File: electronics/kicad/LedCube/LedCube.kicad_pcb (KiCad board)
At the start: 2 copper layers, 86 x 46 mm, 25 parts, among them J1 Conn_01x03, J2 Conn_01x03, J3 Conn_01x03, J4 Conn_01x04, J5 COM, J6 Conn_01x02, J7 JTAG, U3 ESP32-DevKitM

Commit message: Update kicad gerbers
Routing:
- net D0: track 37.2 -> 40.0 mm
- net D1: track 38.6 -> 40.5 mm
- net D3: track 47.2 -> 46.3 mm
- net D2: track 40.1 -> 40.9 mm
- net GND: vias 6 -> 8

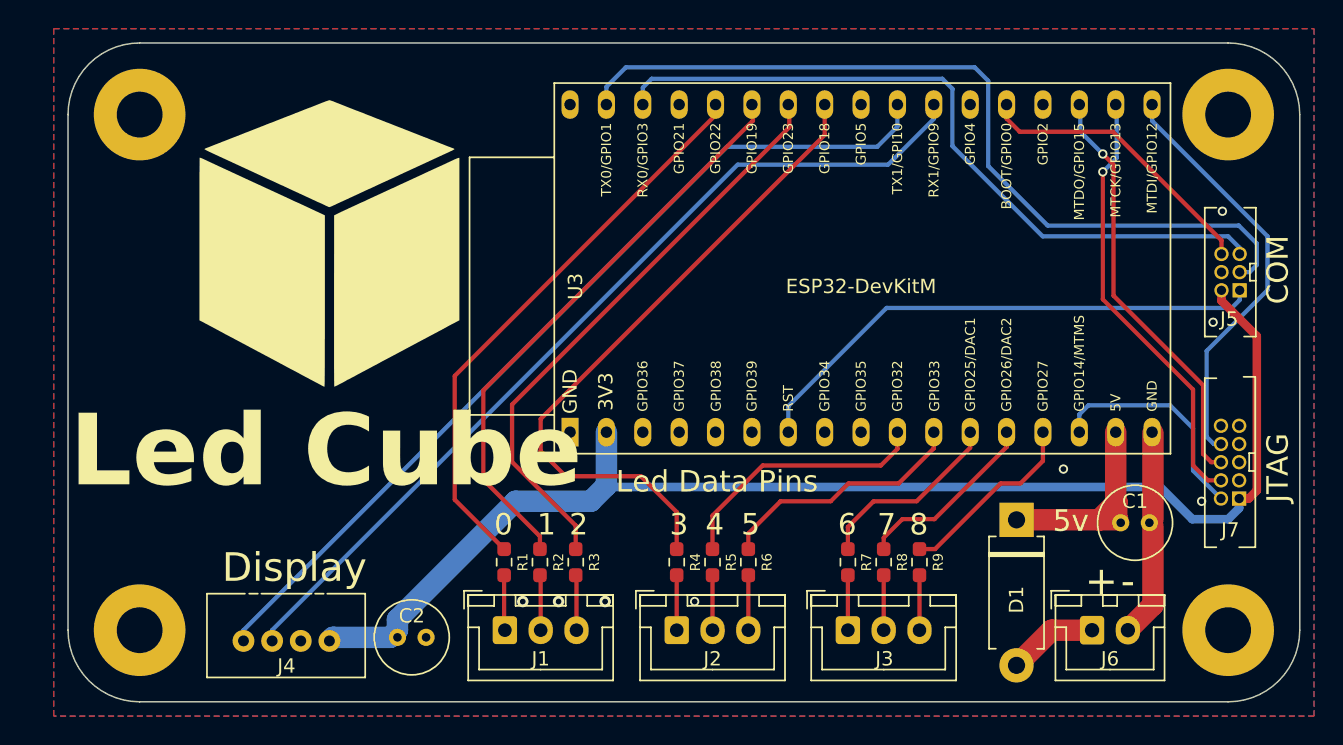
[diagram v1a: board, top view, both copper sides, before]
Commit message: Fix flipped vcc and gnd in KiCad
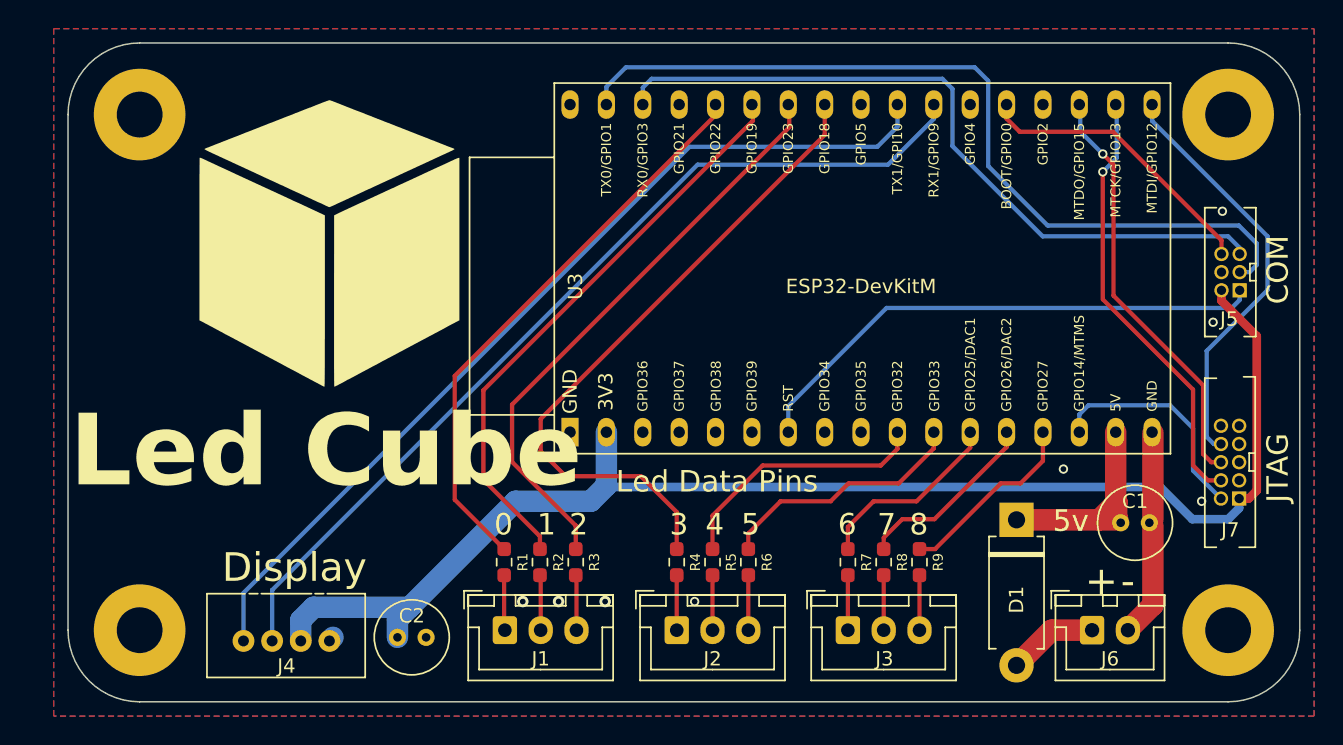
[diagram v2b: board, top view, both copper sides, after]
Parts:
- D1: value D -> 1N4002
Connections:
- J4 pad 1: +3V3 -> GND
- J4 pad 2: GND -> +3V3
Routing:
- net +3V3: track 90.2 -> 95.2 mm
- net UART1_RX: track 62.7 -> 64.4 mm
- net UART1_TX: track 62.5 -> 64.0 mm
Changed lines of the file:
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@@
         (effects (font (size 1 1) (thickness 0.15)))
     )
-    (fp_text value "D" (at 5.08 2.92 90) (layer "F.Fab")
+    (fp_text value "1N4002" (at 5.08 2.92 90) (layer "F.Fab")
         (effects (font (size 1 1) (thickness 0.15)))
     )
@@
       (stroke (width 0.1) (type solid)) (layer "F.Fab"))
     (pad "1" thru_hole circle (at 0 0 270) (size 1.524 1.524) (drill 0.762) (layers "*.Cu" "*.Mask" "F.SilkS")
-      (net 10 "+3V3") (pinfunction "Pin_1") (pintype "passive"))
+      (net 11 "GND") (pinfunction "Pin_1") (pintype "passive"))
     (pad "2" thru_hole circle (at 0 2 270) (size 1.524 1.524) (drill 0.762) (layers "*.Cu" "*.Mask" "F.SilkS")
-      (net 11 "GND") (pinfunction "Pin_2") (pintype "passive"))
+      (net 10 "+3V3") (pinfunction "Pin_2") (pintype "passive"))
     (pad "3" thru_hole circle (at 0 4 270) (size 1.524 1.524) (drill 0.762) (layers "*.Cu" "*.Mask" "F.SilkS")
       (net 12 "UART1_RX") (pinfunction "Pin_3") (pintype "passive"))
@@
   (segment (start 194.69 106.81) (end 194.02 106.81) (width 0.6) (layer "F.Cu") (net 10))
   (segment (start 193.25 108.25) (end 190.75 108.25) (width 0.6) (layer "B.Cu") (net 10))
-  (segment (start 135.25 116) (end 134.75 116.5) (width 1.5) (layer "B.Cu") (net 10))
-  (segment (start 149.84 105.91) (end 148.75 107) (width 1.5) (layer "B.Cu") (net 10))
-  (segment (start 134.75 116.5) (end 130.75 116.5) (width 1.5) (layer "B.Cu") (net 10))
-  (segment (start 135.25 115.25) (end 135.25 116) (width 1.5) (layer "B.Cu") (net 10))
-  (segment (start 130.75 116.5) (end 130.5 116.75) (width 1.5) (layer "B.Cu") (net 10))
-  (segment (start 190.75 108.25) (end 188.5 106) (width 0.6) (layer "B.Cu") (net 10))
+  (segment (start 129.4 114.4) (end 128.5 115.3) (width 1.5) (layer "B.Cu") (net 10))
   (segment (start 148.75 107) (end 143.5 107) (width 1.5) (layer "B.Cu") (net 10))
+  (segment (start 190.75 108.25) (end 188.5 106) (width 0.6) (layer "B.Cu") (net 10))
+  (segment (start 149.84 105.91) (end 148.75 107) (width 1.5) (layer "B.Cu") (net 10))
   (segment (start 194.02 106.81) (end 194.02 107.48) (width 0.6) (layer "B.Cu") (net 10))
-  (segment (start 143.5 107) (end 135.25 115.25) (width 1.5) (layer "B.Cu") (net 10))
+  (segment (start 128.5 115.3) (end 128.5 116.75) (width 1.5) (layer "B.Cu") (net 10))
   (segment (start 149.84 102.175) (end 149.84 105.91) (width 1.5) (layer "B.Cu") (net 10))
   (segment (start 194.02 107.48) (end 193.25 108.25) (width 0.6) (layer "B.Cu") (net 10))
+  (segment (start 143.5 107) (end 136.2 114.3) (width 1.5) (layer "B.Cu") (net 10))
+  (segment (start 136.1 114.4) (end 129.4 114.4) (width 1.5) (layer "B.Cu") (net 10))
+  (segment (start 136.2 114.3) (end 135.25 115.25) (width 1.5) (layer "B.Cu") (net 10))
   (segment (start 188.5 106) (end 150.25 106) (width 0.6) (layer "B.Cu") (net 10))
+  (segment (start 136.2 114.3) (end 136.1 114.4) (width 1.5) (layer "B.Cu") (net 10))
+  (segment (start 135.25 115.25) (end 135.25 116.5) (width 1.5) (layer "B.Cu") (net 10))
   (segment (start 186.25 116) (end 188 114.25) (width 1.5) (layer "F.Cu") (net 11))
   (segment (start 188 108.25) (end 188 102.235) (width 1.5) (layer "F.Cu") (net 11))
@@
   (via (at 192.2 94.5) (size 0.65) (drill 0.4) (layers "F.Cu" "B.Cu") (free) (net 11))
   (via (at 144 114) (size 0.8) (drill 0.4) (layers "F.Cu" "B.Cu") (free) (net 11))
-  (segment (start 159 83.5) (end 169.5 83.5) (width 0.3) (layer "B.Cu") (net 12))
-  (segment (start 126.5 116) (end 159 83.5) (width 0.3) (layer "B.Cu") (net 12))
-  (segment (start 169.5 83.5) (end 172.7 80.3) (width 0.3) (layer "B.Cu") (net 12))
+  (segment (start 130.75 116.5) (end 130.5 116.75) (width 1.5) (layer "B.Cu") (net 11))
   (segment (start 172.7 80.3) (end 172.7 79.3) (width 0.3) (layer "B.Cu") (net 12))
-  (segment (start 126.5 116.75) (end 126.5 116) (width 0.3) (layer "B.Cu") (net 12))
-  (segment (start 124.5 116) (end 124.5 116.75) (width 0.3) (layer "B.Cu") (net 13))
+  (segment (start 169.5 83.5) (end 172.7 80.3) (width 0.3) (layer "B.Cu") (net 12))
+  (segment (start 126.5 116.75) (end 126.5 113.2) (width 0.3) (layer "B.Cu") (net 12))
+  (segment (start 126.5 113.2) (end 156.2 83.5) (width 0.3) (layer "B.Cu") (net 12))
+  (segment (start 156.2 83.5) (end 169.5 83.5) (width 0.3) (layer "B.Cu") (net 12))
   (segment (start 170.16 80.84) (end 168.75 82.25) (width 0.3) (layer "B.Cu") (net 13))
-  (segment (start 168.75 82.25) (end 158.25 82.25) (width 0.3) (layer "B.Cu") (net 13))
+  (segment (start 168.75 82.25) (end 155.65 82.25) (width 0.3) (layer "B.Cu") (net 13))
   (segment (start 170.16 79.3) (end 170.16 80.84) (width 0.3) (layer "B.Cu") (net 13))
-  (segment (start 158.25 82.25) (end 124.5 116) (width 0.3) (layer "B.Cu") (net 13))
+  (segment (start 155.65 82.25) (end 124.5 113.4) (width 0.3) (layer "B.Cu") (net 13))
+  (segment (start 124.5 113.4) (end 124.5 116.75) (width 0.3) (layer "B.Cu") (net 13))
   (segment (start 162.54 100.36) (end 162.54 102.175) (width 0.3) (layer "B.Cu") (net 14))
   (segment (start 194.055 92.27) (end 194.055 92.945) (width 0.3) (layer "B.Cu") (net 14))
